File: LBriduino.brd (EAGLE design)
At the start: 45.4 x 27.9 mm, 12 parts, among them J1 105017-0001

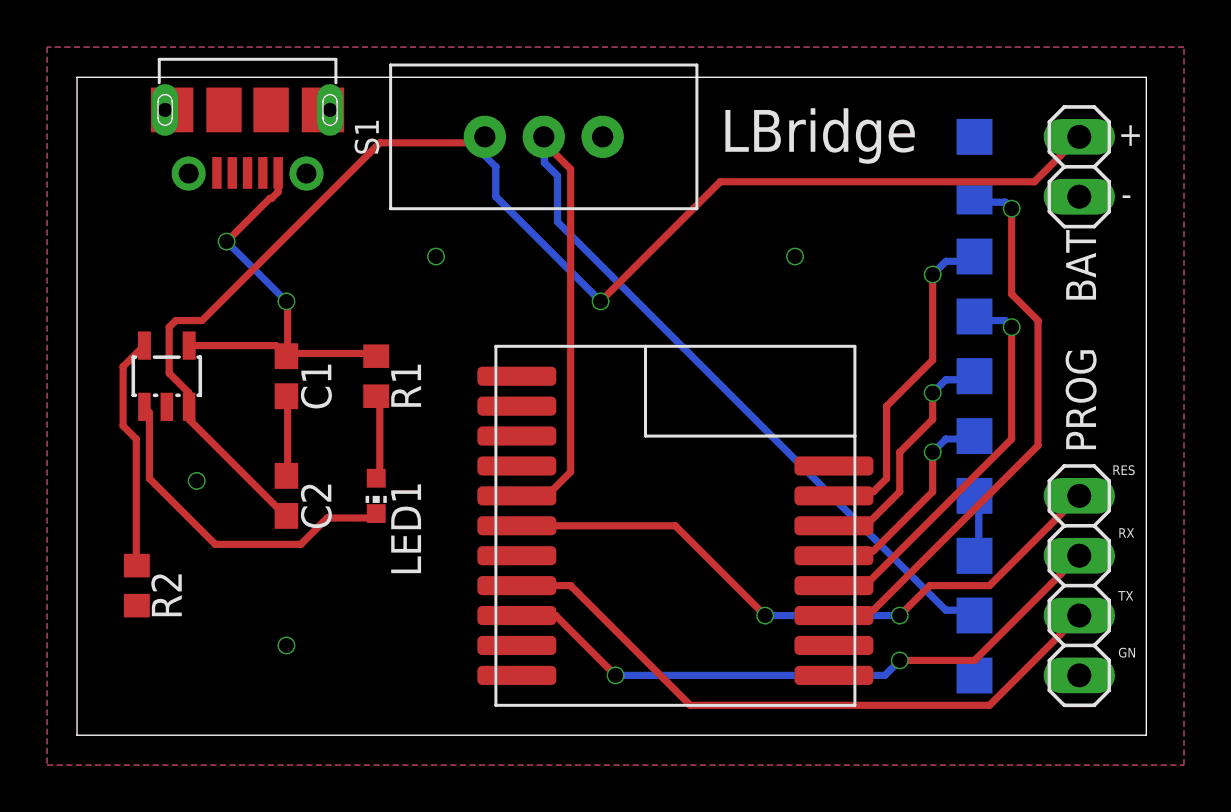
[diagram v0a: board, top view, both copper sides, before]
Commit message: minor re-wireing, updated pic, specified usb connector in description
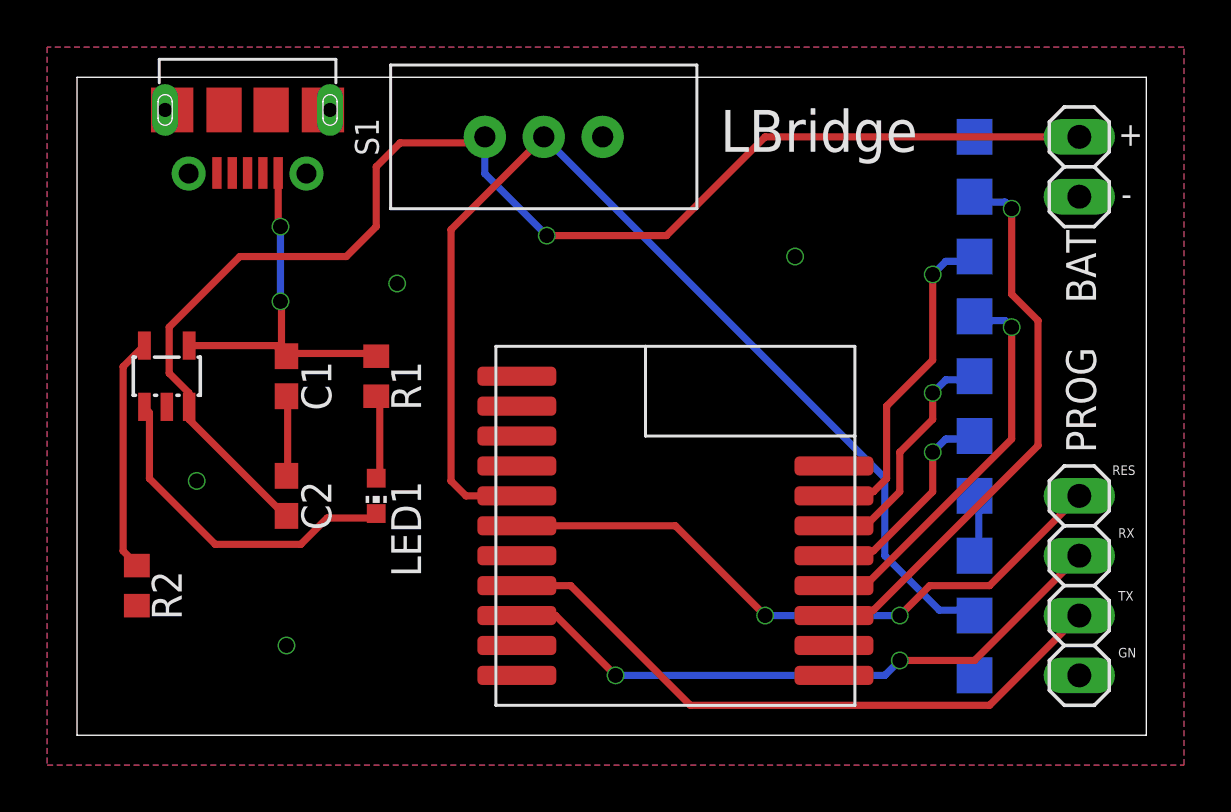
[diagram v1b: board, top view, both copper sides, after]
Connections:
- net GND: now also U$1.P$8
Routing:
- net SWITCH: track 46.0 -> 49.6 mm
- net +5V: track 17.9 -> 15.9 mm
- net VCC: track 59.3 -> 57.9 mm
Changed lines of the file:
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@@
 <wire x1="8.9408" y1="16.2052" x2="8.89" y2="16.09" width="0.3048" layer="1"/>
 <wire x1="12.573" y1="16.2052" x2="12.7" y2="16.09" width="0.3048" layer="1"/>
-<via x="6.35" y="20.955" extent="1-16" drill="0.635"/>
-<via x="8.89" y="18.415" extent="1-16" drill="0.635"/>
-<wire x1="6.35" y1="20.955" x2="8.1816" y2="22.7866" width="0.3048" layer="1"/>
-<wire x1="8.1816" y1="22.7866" x2="8.2573375" y2="22.7866" width="0.3048" layer="1"/>
-<wire x1="8.2573375" y1="22.7866" x2="8.539" y2="23.0682625" width="0.3048" layer="1"/>
-<wire x1="8.539" y1="23.0682625" x2="8.539" y2="23.868" width="0.3048" layer="1"/>
-<wire x1="8.89" y1="18.415" x2="8.9408" y2="18.3642" width="0.3048" layer="1"/>
-<wire x1="8.9408" y1="18.3642" x2="8.9408" y2="16.2052" width="0.3048" layer="1"/>
-<wire x1="6.35" y1="20.955" x2="8.89" y2="18.415" width="0.3048" layer="16"/>
-<wire x1="8.89" y1="16.09" x2="8.44" y2="16.54" width="0.3048" layer="1"/>
+<via x="8.636" y="21.59" extent="1-16" drill="0.635"/>
+<via x="8.636" y="18.415" extent="1-16" drill="0.635"/>
+<wire x1="8.68" y1="16.3" x2="8.89" y2="16.09" width="0.3048" layer="1"/>
+<wire x1="8.68" y1="16.3" x2="8.44" y2="16.54" width="0.3048" layer="1"/>
 <wire x1="8.44" y1="16.54" x2="4.76" y2="16.54" width="0.3048" layer="1"/>
+<wire x1="8.539" y1="21.62" x2="8.636" y2="21.59" width="0.3048" layer="1"/>
+<wire x1="8.539" y1="21.62" x2="8.539" y2="23.868" width="0.3048" layer="1"/>
+<wire x1="8.636" y1="21.59" x2="8.636" y2="18.415" width="0.3048" layer="16"/>
+<wire x1="8.636" y1="18.415" x2="8.68" y2="18.244" width="0.3048" layer="1"/>
+<wire x1="8.68" y1="18.244" x2="8.68" y2="16.3" width="0.3048" layer="1"/>
 </signal>
 <signal name="N$6">
 <contactref element="U$2" pad="5"/>
 <contactref element="R2" pad="1"/>
-<wire x1="2.5146" y1="12.573" x2="2.5146" y2="7.2644" width="0.3048" layer="1"/>
-<wire x1="1.9558" y1="13.1318" x2="2.5146" y2="12.573" width="0.3048" layer="1"/>
-<wire x1="1.9558" y1="15.6464" x2="1.9558" y2="13.1318" width="0.3048" layer="1"/>
 <wire x1="2.794" y1="16.4846" x2="1.9558" y2="15.6464" width="0.3048" layer="1"/>
 <wire x1="2.5146" y1="7.2644" x2="2.54" y2="7.2" width="0.3048" layer="1"/>
 <wire x1="2.794" y1="16.4846" x2="2.86" y2="16.54" width="0.3048" layer="1"/>
+<wire x1="1.9558" y1="7.8232" x2="2.5146" y2="7.2644" width="0.3048" layer="1"/>
+<wire x1="1.9558" y1="15.6464" x2="1.9558" y2="7.8232" width="0.3048" layer="1"/>
 </signal>
 <signal name="GND">
@@
 <via x="5.08" y="10.795" extent="1-16" drill="0.635"/>
 <via x="8.89" y="3.81" extent="1-16" drill="0.635"/>
-<via x="15.24" y="20.32" extent="1-16" drill="0.635"/>
+<via x="13.589" y="19.177" extent="1-16" drill="0.635"/>
 <contactref element="PROG" pad="1"/>
 <contactref element="BAT" pad="1"/>
 <via x="30.48" y="20.32" extent="1-16" drill="0.635"/>
+<contactref element="U$1" pad="P$8"/>
 </signal>
 <signal name="VCC">
@@
 <wire x1="8.6614" y1="9.4996" x2="8.89" y2="9.31" width="0.3048" layer="1"/>
 <wire x1="4.7498" y1="13.6906" x2="4.76" y2="13.94" width="0.3048" layer="1"/>
-<wire x1="12.8524" y1="25.146" x2="17.0434" y2="25.146" width="0.3048" layer="1"/>
-<wire x1="5.3086" y1="17.6022" x2="12.8524" y2="25.146" width="0.3048" layer="1"/>
-<wire x1="4.191" y1="17.6022" x2="5.3086" y2="17.6022" width="0.3048" layer="1"/>
-<wire x1="3.9116" y1="17.3228" x2="4.191" y2="17.6022" width="0.3048" layer="1"/>
 <wire x1="3.9116" y1="15.367" x2="3.9116" y2="17.3228" width="0.3048" layer="1"/>
 <wire x1="4.7498" y1="14.5288" x2="3.9116" y2="15.367" width="0.3048" layer="1"/>
@@
 <wire x1="4.7498" y1="13.97" x2="4.76" y2="13.94" width="0.3048" layer="1"/>
 <contactref element="BAT" pad="2"/>
-<wire x1="40.64" y1="23.495" x2="42.545" y2="25.4" width="0.3048" layer="1"/>
-<wire x1="27.305" y1="23.495" x2="40.64" y2="23.495" width="0.3048" layer="1"/>
-<wire x1="22.225" y1="18.415" x2="27.305" y2="23.495" width="0.3048" layer="1"/>
-<wire x1="17.78" y1="22.86" x2="22.225" y2="18.415" width="0.3048" layer="16"/>
-<wire x1="17.78" y1="24.13" x2="17.78" y2="22.86" width="0.3048" layer="16"/>
-<wire x1="17.145" y1="24.765" x2="17.78" y2="24.13" width="0.3048" layer="16"/>
-<wire x1="17.145" y1="25.4" x2="17.145" y2="24.765" width="0.3048" layer="16"/>
-<wire x1="17.145" y1="25.4" x2="17.312" y2="25.4" width="0.3048" layer="16"/>
-<via x="22.225" y="18.415" extent="1-16" drill="0.635"/>
+<via x="19.939" y="21.209" extent="1-16" drill="0.635"/>
+<wire x1="3.9116" y1="17.3228" x2="6.9088" y2="20.32" width="0.3048" layer="1"/>
+<wire x1="6.9088" y1="20.32" x2="11.43" y2="20.32" width="0.3048" layer="1"/>
+<wire x1="11.43" y1="20.32" x2="12.7" y2="21.59" width="0.3048" layer="1"/>
+<wire x1="12.7" y1="21.59" x2="12.7" y2="24.13" width="0.3048" layer="1"/>
+<wire x1="12.7" y1="24.13" x2="13.716" y2="25.146" width="0.3048" layer="1"/>
+<wire x1="13.716" y1="25.146" x2="17.0434" y2="25.146" width="0.3048" layer="1"/>
+<wire x1="42.545" y1="25.4" x2="29.21" y2="25.4" width="0.3048" layer="1"/>
+<wire x1="29.21" y1="25.4" x2="25.019" y2="21.209" width="0.3048" layer="1"/>
+<wire x1="25.019" y1="21.209" x2="19.939" y2="21.209" width="0.3048" layer="1"/>
+<wire x1="19.939" y1="21.209" x2="17.312" y2="23.836" width="0.3048" layer="16"/>
+<wire x1="17.312" y1="23.836" x2="17.312" y2="25.4" width="0.3048" layer="16"/>
 </signal>
 <signal name="N$3">
@@
 <contactref element="U$1" pad="P$13"/>
 <contactref element="S1" pad="2"/>
-<wire x1="36.8808" y1="5.3086" x2="37.9984" y2="5.3086" width="0.3048" layer="16"/>
-<wire x1="20.3962" y1="21.7932" x2="36.8808" y2="5.3086" width="0.3048" layer="16"/>
-<wire x1="20.3962" y1="23.749" x2="20.3962" y2="21.7932" width="0.3048" layer="16"/>
-<wire x1="19.8374" y1="24.3078" x2="20.3962" y2="23.749" width="0.3048" layer="16"/>
-<wire x1="19.8374" y1="25.146" x2="19.8374" y2="24.3078" width="0.3048" layer="16"/>
-<wire x1="37.9984" y1="5.3086" x2="38.1" y2="5.08" width="0.3048" layer="16"/>
-<wire x1="19.8374" y1="25.146" x2="19.812" y2="25.4" width="0.3048" layer="16"/>
+<wire x1="38.1" y1="5.08" x2="37.9984" y2="5.3086" width="0.3048" layer="16"/>
 <wire x1="20.1168" y1="10.3378" x2="18.7198" y2="10.3378" width="0.3048" layer="1"/>
-<wire x1="20.955" y1="11.176" x2="20.1168" y2="10.3378" width="0.3048" layer="1"/>
-<wire x1="20.955" y1="24.0284" x2="20.955" y2="11.176" width="0.3048" layer="1"/>
-<wire x1="19.8374" y1="25.146" x2="20.955" y2="24.0284" width="0.3048" layer="1"/>
 <wire x1="18.7198" y1="10.3378" x2="18.669" y2="10.16" width="0.3048" layer="1"/>
-<wire x1="19.8374" y1="25.146" x2="19.812" y2="25.4" width="0.3048" layer="1"/>
+<wire x1="18.669" y1="10.16" x2="16.51" y2="10.16" width="0.3048" layer="1"/>
+<wire x1="16.51" y1="10.16" x2="15.875" y2="10.795" width="0.3048" layer="1"/>
+<wire x1="15.875" y1="21.463" x2="19.812" y2="25.4" width="0.3048" layer="1"/>
+<wire x1="15.875" y1="10.795" x2="15.875" y2="21.463" width="0.3048" layer="1"/>
+<wire x1="36.6014" y1="5.3086" x2="34.29" y2="7.62" width="0.3048" layer="16"/>
+<wire x1="37.9984" y1="5.3086" x2="36.6014" y2="5.3086" width="0.3048" layer="16"/>
+<wire x1="34.29" y1="7.62" x2="34.29" y2="10.922" width="0.3048" layer="16"/>
+<wire x1="34.29" y1="10.922" x2="19.812" y2="25.4" width="0.3048" layer="16"/>
 </signal>
 <signal name="P.TXD">

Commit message: reduced groundplane, used traces instead
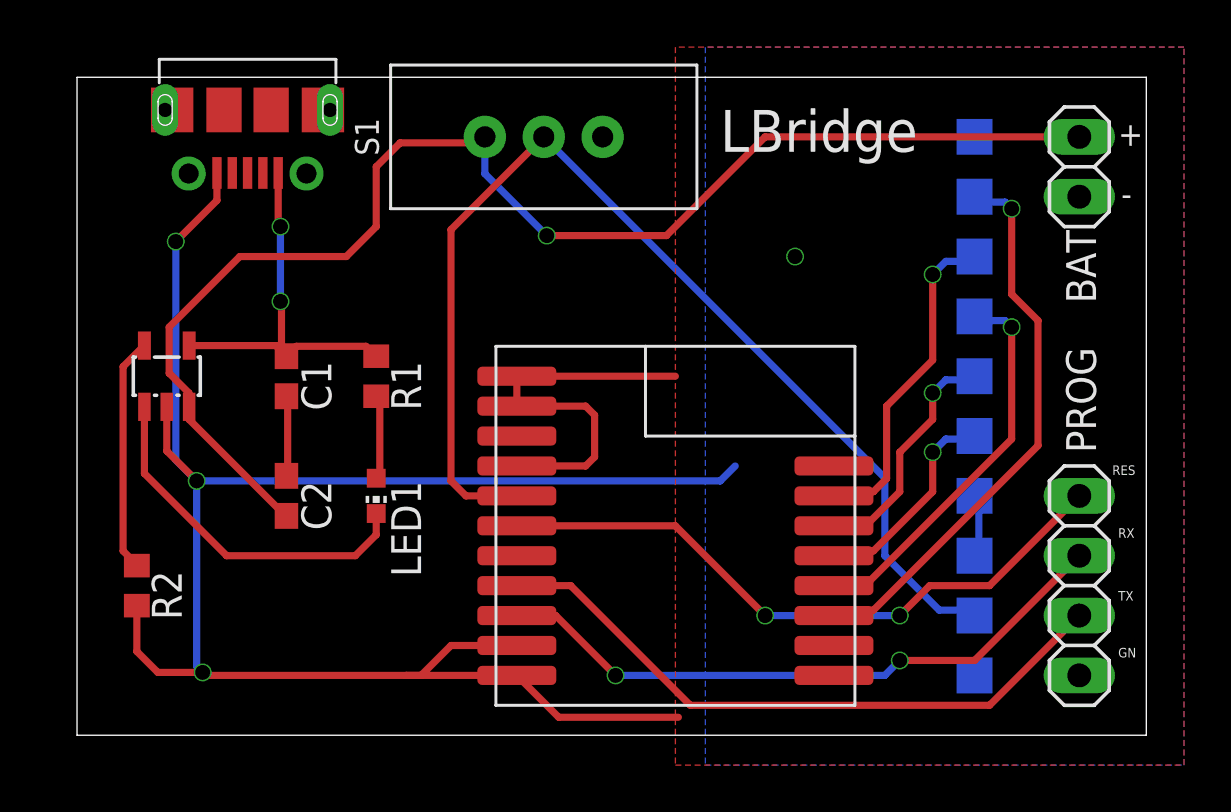
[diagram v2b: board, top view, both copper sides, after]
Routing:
- net GND: track 0.00 -> 97.2 mm
- net N$2: track 14.5 -> 15.6 mm
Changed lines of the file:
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@@
 <contactref element="LED1" pad="C"/>
 <contactref element="U$2" pad="1"/>
-<wire x1="10.6172" y1="9.2202" x2="12.573" y2="9.2202" width="0.3048" layer="1"/>
-<wire x1="10.6172" y1="9.2202" x2="9.4996" y2="8.1026" width="0.3048" layer="1"/>
 <wire x1="12.573" y1="9.2202" x2="12.7" y2="9.41" width="0.3048" layer="1"/>
-<wire x1="2.86" y1="13.94" x2="3.0734" y2="13.6906" width="0.3048" layer="1"/>
-<wire x1="3.0734" y1="10.8966" x2="3.0734" y2="13.6906" width="0.3048" layer="1"/>
-<wire x1="9.4996" y1="8.1026" x2="5.8674" y2="8.1026" width="0.3048" layer="1"/>
-<wire x1="5.8674" y1="8.1026" x2="3.0734" y2="10.8966" width="0.3048" layer="1"/>
+<wire x1="12.7" y1="9.41" x2="12.7" y2="8.509" width="0.3048" layer="1"/>
+<wire x1="12.7" y1="8.509" x2="11.811" y2="7.62" width="0.3048" layer="1"/>
+<wire x1="11.811" y1="7.62" x2="6.35" y2="7.62" width="0.3048" layer="1"/>
+<wire x1="2.86" y1="11.11" x2="2.86" y2="13.94" width="0.3048" layer="1"/>
+<wire x1="6.35" y1="7.62" x2="2.86" y2="11.11" width="0.3048" layer="1"/>
 </signal>
 <signal name="N$4">
@@
 <contactref element="U$2" pad="4"/>
 <contactref element="J1" pad="1"/>
-<wire x1="8.9408" y1="16.2052" x2="12.573" y2="16.2052" width="0.3048" layer="1"/>
 <wire x1="8.9408" y1="16.2052" x2="8.89" y2="16.09" width="0.3048" layer="1"/>
 <wire x1="12.573" y1="16.2052" x2="12.7" y2="16.09" width="0.3048" layer="1"/>
@@
 <wire x1="8.636" y1="18.415" x2="8.68" y2="18.244" width="0.3048" layer="1"/>
 <wire x1="8.68" y1="18.244" x2="8.68" y2="16.3" width="0.3048" layer="1"/>
+<wire x1="8.89" y1="16.09" x2="9.31" y2="16.51" width="0.3048" layer="1"/>
+<wire x1="12.2682" y1="16.51" x2="12.573" y2="16.2052" width="0.3048" layer="1"/>
+<wire x1="9.31" y1="16.51" x2="12.2682" y2="16.51" width="0.3048" layer="1"/>
 </signal>
 <signal name="N$6">
@@
 <contactref element="U$1" pad="P$19"/>
 <polygon width="0.1524" layer="1">
-<vertex x="-1.27" y="29.21"/>
-<vertex x="-1.27" y="-1.27"/>
+<vertex x="25.4" y="29.21"/>
+<vertex x="25.4" y="-1.27"/>
 <vertex x="46.99" y="-1.27"/>
 <vertex x="46.99" y="29.21"/>
 </polygon>
 <polygon width="0.1524" layer="16">
-<vertex x="-1.27" y="29.21"/>
-<vertex x="-1.27" y="-1.27"/>
+<vertex x="26.67" y="29.21"/>
+<vertex x="26.67" y="-1.27"/>
 <vertex x="46.99" y="-1.27"/>
 <vertex x="46.99" y="29.21"/>
 </polygon>
 <via x="5.08" y="10.795" extent="1-16" drill="0.635"/>
-<via x="8.89" y="3.81" extent="1-16" drill="0.635"/>
-<via x="13.589" y="19.177" extent="1-16" drill="0.635"/>
 <contactref element="PROG" pad="1"/>
 <contactref element="BAT" pad="1"/>
 <via x="30.48" y="20.32" extent="1-16" drill="0.635"/>
 <contactref element="U$1" pad="P$8"/>
+<wire x1="25.4" y1="15.24" x2="18.669" y2="15.24" width="0.3048" layer="1"/>
+<wire x1="18.669" y1="15.24" x2="18.669" y2="13.97" width="0.3048" layer="1"/>
+<wire x1="18.669" y1="13.97" x2="21.59" y2="13.97" width="0.3048" layer="1"/>
+<wire x1="21.59" y1="13.97" x2="21.971" y2="13.589" width="0.3048" layer="1"/>
+<wire x1="21.971" y1="11.811" x2="21.59" y2="11.43" width="0.3048" layer="1"/>
+<wire x1="21.971" y1="13.589" x2="21.971" y2="11.811" width="0.3048" layer="1"/>
+<via x="4.191" y="20.955" extent="1-16" drill="0.635"/>
+<wire x1="5.939" y1="23.868" x2="5.939" y2="22.703" width="0.3048" layer="1"/>
+<wire x1="5.939" y1="22.703" x2="4.191" y2="20.955" width="0.3048" layer="1"/>
+<wire x1="4.191" y1="20.955" x2="4.191" y2="11.684" width="0.3048" layer="16"/>
+<wire x1="4.191" y1="11.684" x2="5.08" y2="10.795" width="0.3048" layer="16"/>
+<via x="5.334" y="2.667" extent="1-16" drill="0.635"/>
+<wire x1="5.08" y1="10.795" x2="5.08" y2="2.921" width="0.3048" layer="16"/>
+<wire x1="5.08" y1="2.921" x2="5.334" y2="2.667" width="0.3048" layer="16"/>
+<wire x1="3.429" y1="2.667" x2="5.334" y2="2.667" width="0.3048" layer="1"/>
+<wire x1="2.54" y1="3.556" x2="2.54" y2="5.5" width="0.3048" layer="1"/>
+<wire x1="3.429" y1="2.667" x2="2.54" y2="3.556" width="0.3048" layer="1"/>
+<wire x1="5.334" y1="2.667" x2="5.461" y2="2.54" width="0.3048" layer="1"/>
+<wire x1="13.97" y1="2.54" x2="5.461" y2="2.54" width="0.3048" layer="1"/>
+<wire x1="13.97" y1="2.54" x2="18.669" y2="2.54" width="0.3048" layer="1"/>
+<wire x1="18.669" y1="3.81" x2="15.875" y2="3.81" width="0.3048" layer="1"/>
+<wire x1="15.875" y1="3.81" x2="14.605" y2="2.54" width="0.3048" layer="1"/>
+<wire x1="14.605" y1="2.54" x2="13.97" y2="2.54" width="0.3048" layer="1"/>
+<wire x1="18.669" y1="2.54" x2="20.447" y2="0.762" width="0.3048" layer="1"/>
+<wire x1="20.447" y1="0.762" x2="25.527" y2="0.762" width="0.3048" layer="1"/>
+<wire x1="5.08" y1="10.795" x2="3.81" y2="12.065" width="0.3048" layer="1"/>
+<wire x1="3.81" y1="12.065" x2="3.81" y2="13.94" width="0.3048" layer="1"/>
+<wire x1="21.59" y1="11.43" x2="18.669" y2="11.43" width="0.3048" layer="1"/>
+<wire x1="5.08" y1="10.795" x2="27.305" y2="10.795" width="0.3048" layer="16"/>
+<wire x1="27.305" y1="10.795" x2="27.94" y2="11.43" width="0.3048" layer="16"/>
 </signal>
 <signal name="VCC">

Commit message: changed BM019 voltage input from VIN to VDD, added testing points for ampere meter in off-mode
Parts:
- added C3: 100nF, resistor:C0603
- C1, C2: value 4.7µ -> 4.7µF
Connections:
- net N$3 renamed SCK
- net N$5 renamed MOSI
- net N$7 renamed MISO
- net N$8 renamed SS
- net N$9 renamed IRQ
- removed net N$10: BM2.SS0, BM2.VDD
- new net N$3: C3.2, PROG.4
- new net TEST: S1.3
- net P.RESET: now also C3.1; no longer PROG.4
- net SWITCH: now also BM2.SS0, BM2.VDD; no longer BM2.VIN
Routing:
- net N$3: track 0.00 -> 44.0 mm, vias 0 -> 1
- net P.RESET: track 27.6 -> 7.97 mm, vias 2 -> 0
- net TEST: track 0.00 -> 9.75 mm, vias 0 -> 1
- net VCC: track 57.9 -> 61.8 mm, vias 1 -> 2
- net N$10: track 2.71 -> 0.00 mm
- net GND: track 97.2 -> 95.7 mm
- net SWITCH: track 49.6 -> 48.5 mm
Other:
- board text added: "TEST"
